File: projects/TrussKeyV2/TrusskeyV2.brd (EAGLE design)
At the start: 39.6 x 19 mm, 43 parts, among them J1 M20-9980346, J2 XF2L-0535-1, J3 10104111-0001LF, Q1 ABM-16MHZ, SW1 LS12T2-T, SW2 EVQ11U09K, SW3 ESE31L11T, U2 TPS62200, U3 LC709203, U5 MCP73831T-2ACI/OT, X1 CON-1PIN, X3 CON-1PIN

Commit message: TrussKey v2
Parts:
- removed JP2: Solenoid, jumper:JP1
- added X2, X4: CON-1PIN, NewPart:CON-1PIN
- moved X3 1.41 mm to (26.7, 13.5)
- moved R15 0.76 mm to (33.4, 10.1)
- moved Q2 0.71 mm to (26.2, 11.1)
- moved U3 0.64 mm to (30.5, 8.92)
- moved SW3 0.45 mm to (36.3, 15.3)
- moved R16 0.24 mm to (32.6, 13.8)
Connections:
- net N$9: now also X4.P$1; no longer JP2.1
- net VCC: now also X2.P$1; no longer JP2.2
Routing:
- net SDA: track 20.0 -> 29.9 mm, vias 3 -> 5
- net SCL: track 20.9 -> 30.0 mm, vias 0 -> 1
- net VCC: track 88.1 -> 92.5 mm, vias 3 -> 4
- net DETSW: track 42.7 -> 45.5 mm
- net N$10: track 10.6 -> 9.89 mm

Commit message: V2 PCB
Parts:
- removed X2, X4: CON-1PIN, NewPart:CON-1PIN
- added J4, J5: 5-146280-1, 5-146280-1:HDRV1W67P0X254_1X1_213X234X821
- moved X1 1.21 mm to (25.7, 16.7), flipped to the bottom, turned to 270 degrees
- moved X3 0.54 mm to (26.4, 13.1)
- moved Q2 0.49 mm to (26.3, 10.6)
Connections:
- net N$9: now also J5.1; no longer X4.P$1
- net VCC: now also J4.1; no longer X2.P$1
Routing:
- net VCC: track 92.5 -> 82.8 mm
- net SDA: track 29.9 -> 32.0 mm
- net DETSW: track 45.5 -> 43.8 mm
- net VBUS2: track 6.02 -> 6.85 mm
- net GND: track 58.7 -> 58.8 mm, vias 7 -> 8

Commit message: FPC changed
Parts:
- removed J2: XF2L-0535-1, adafruit:XF2L-0535-1
- added J6: MOLEX_503480-0600MOLEX_503480-0600_0_0, Molex - 503480-0600:MOLEX_503480-0600_0
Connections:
- net GND: now also J6.5; no longer J2.5
- net REST: now also J6.2; no longer J2.2
- net RX: now also J6.4; no longer J2.4
- net TX: now also J6.3; no longer J2.3
- net VCC: now also J6.1; no longer J2.1
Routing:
- net VCC: track 82.8 -> 82.2 mm

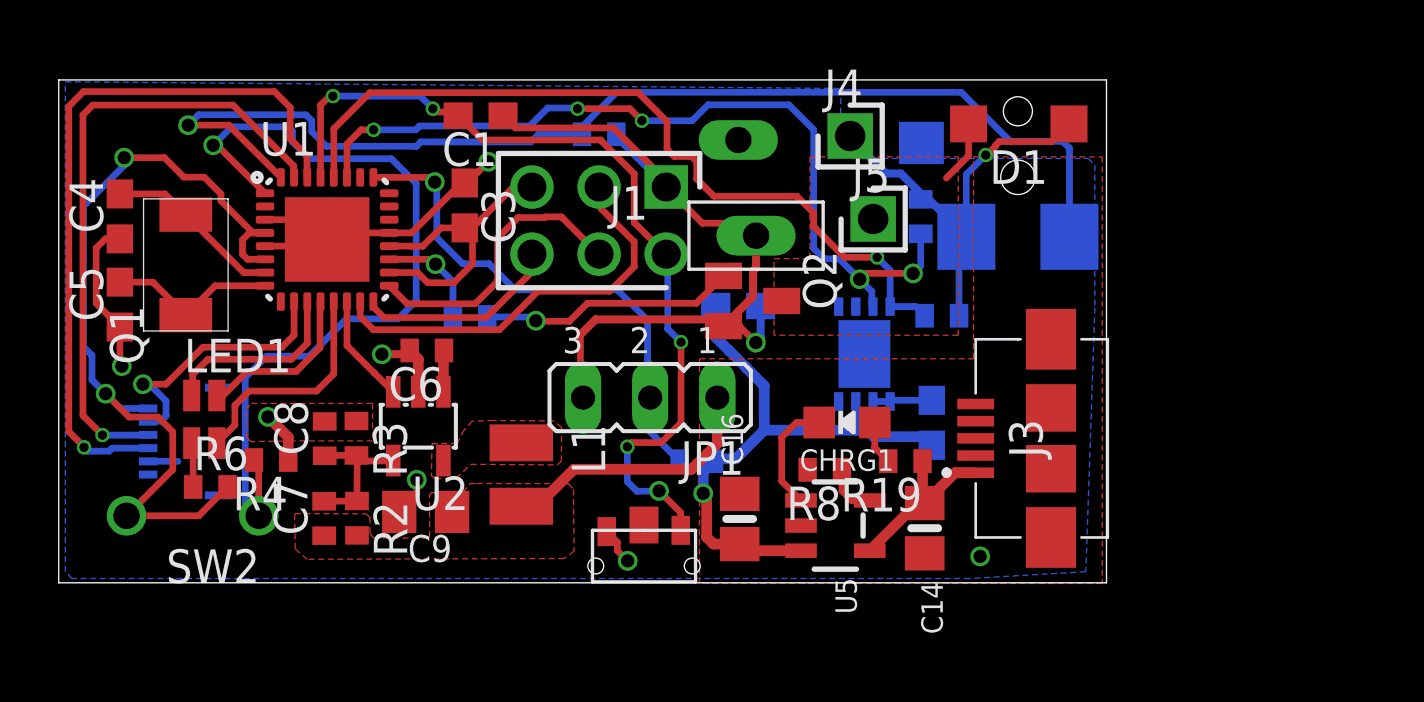
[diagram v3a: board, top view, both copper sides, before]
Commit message: Gas Gauge change
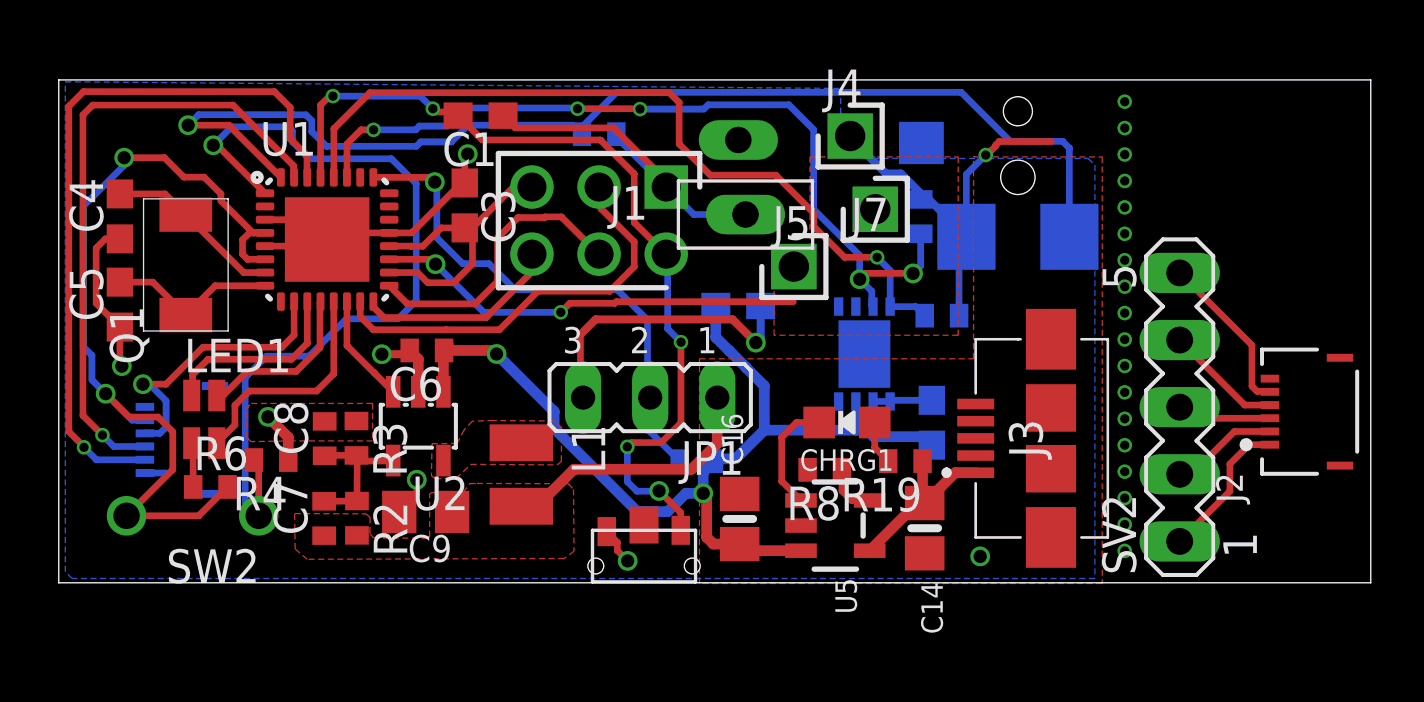
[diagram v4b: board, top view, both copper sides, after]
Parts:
- removed D1: (no value), diode:SOD123
- removed Q2: (no value), semicon-smd-ipc:SOT23
- removed R5: 2.2K, resistor:R0402
- added J2: MOLEX_503480-0600MOLEX_503480-0600_0_0, Molex - 503480-0600:MOLEX_503480-0600_0
- added J7: 5-146280-1, 5-146280-1:HDRV1W67P0X254_1X1_213X234X821
- added SV2: (no value), con-lstb:MA05-1
- moved J5 3.50 mm to (27.8, 11.9)
- moved X3 0.89 mm to (26.0, 13.9)
- moved J6 0.13 mm to (4.59, 5.37)
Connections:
- removed net N$10: Q2.1, R5.1
- removed net N$7: C6.1, U2.1
- removed net N$9: D1.A, J5.1, Q2.3
- removed net SOL: R5.2, U1.19
- new net GNDSIM: J2.5, SV2.5
- new net RESTSIM: J2.2, SV2.2
- new net RXSIM: J2.4, SV2.4
- new net SERV: J7.1, U1.19
- new net TXSIM: J2.3, SV2.3
- new net VCCSIM: J2.1, SV2.1
- net GND: now also J5.1, J6.6; no longer J6.5, Q2.2
- net REST: now also J6.3; no longer J6.2
- net RX: now also J6.5; no longer J6.4
- net TX: now also J6.4; no longer J6.3
- net VCC: now also C6.1, J6.2, U2.1; no longer D1.C, J6.1
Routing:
- net SERV: track 0.00 -> 16.3 mm, vias 0 -> 2
- net VCC: track 82.2 -> 96.1 mm, vias 4 -> 5
- net N$10: track 9.72 -> 0.00 mm, vias 1 -> 0
- net GNDSIM: track 0.00 -> 6.19 mm
- net VCCSIM: track 0.00 -> 5.53 mm
- net GND: track 58.8 -> 53.8 mm
- net RXSIM: track 0.00 -> 4.43 mm
- net SOL: track 4.10 -> 0.00 mm, vias 1 -> 0
- net RESTSIM: track 0.00 -> 4.09 mm
- net TXSIM: track 0.00 -> 3.59 mm
- net N$9: track 2.40 -> 0.00 mm
- net N$7: track 1.58 -> 0.00 mm, vias 0 -> 1
- net SDA: track 32.0 -> 31.3 mm
- net REST: track 10.2 -> 10.8 mm
- added copper zone on layer 1, net SERV
- removed copper zone on layer 1, net N$9
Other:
- board size 39.6 x 19 mm -> 49.6 x 19 mm

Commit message: GasGauge
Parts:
- removed C17: 1uF, rcl:C0603
- removed R15, R16: 10K, resistor:R0402
- removed U3: LC709203, NewPart:WDFN8
- added C10: 1uF, rcl:C0603
- added C11: 10nF, rcl:C0603
- added IC1: MAX17043X+T10, SamacSys_Parts:BGA9C40P3X3_160X142X69
- added R10, R5: 4.7K, resistor:R0402
- added R11: 180, resistor:R0402
- added R9: 1K, resistor:R0402
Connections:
- new net N$10: C10.1, IC1.B3, R9.2
- new net N$9: C11.1, IC1.C2, R11.2
- net GND: now also C10.2, C11.2, IC1.A3, IC1.B1, IC1.C3; no longer C17.1, U3.1, U3.2, U3.9
- net SCL: now also IC1.A2, R10.1; no longer R15.1, U3.8
- net SDA: now also IC1.A1, R5.1; no longer R16.1, U3.7
- net VCC: now also R10.2, R11.1, R5.2, R9.1; no longer C17.2, R15.2, R16.2, U3.3
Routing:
- net VCC: track 96.1 -> 87.2 mm
- net N$9: track 0.00 -> 5.23 mm
- net N$10: track 0.00 -> 3.28 mm
- net GND: track 53.8 -> 55.3 mm, vias 8 -> 9
